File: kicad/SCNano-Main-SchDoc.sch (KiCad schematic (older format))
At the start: 26 parts, among them CON1 SC_CON_GEIGIE_4PIN, IC1 SN74LV4052A, Q1 STU85N3LH5, Q2 STU85N3LH5, Q3 STU85N3LH5, Q4 STU85N3LH5, SW1 SW-DPDT

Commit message: Remove alternate-mode symbols in RedBear Altium schematic symbols to prevent overlapped symbols in converted KiCAD schematic
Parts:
- removed IC12: (no value), symbol CAP_POL_RB13-25
- added 3V3, 3V3_10, 3V3_11, 3V3_2, 3V3_3, 3V3_4, 3V3_5, 3V3_6, 3V3_7, 3V3_8, 3V3_9: +3V3, symbol 3V3
- added GND, GND_10, GND_11, GND_12, GND_13, GND_14, GND_15, GND_2, GND_3, GND_4, GND_5, GND_6, GND_7, GND_8, GND_9: +GND, symbol GND
- added IC: (no value), symbol CAP_POL_RB13-25
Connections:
- net labels removed: +3V3, +GND

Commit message: Some more fixes for symbol related issues
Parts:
- removed 3V3, 3V3_10, 3V3_11, 3V3_2, 3V3_3, 3V3_4, 3V3_5, 3V3_6, 3V3_7, 3V3_8, 3V3_9: +3V3, symbol 3V3
- removed GND, GND_10, GND_11, GND_12, GND_13, GND_14, GND_15, GND_2, GND_3, GND_4, GND_5, GND_6, GND_7, GND_8, GND_9: +GND, symbol GND
- removed IC: (no value), symbol CAP_POL_RB13-25
- removed SOLARPANEL: VOLTAIC_SOLAR_PANEL_1W, symbol VOLTAIC_SOLAR_PANEL_1W
- added C1: CAP POL RB13-25, symbol CAP_POL_RB13-25
- added SOLARPANEL1: VOLTAIC_SOLAR_PANEL_1W, symbol VOLTAIC_SOLAR_PANEL_1W
- J1: value (none) -> ~
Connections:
- net labels added: +3V3, +GND
- wire segments 135 -> 122

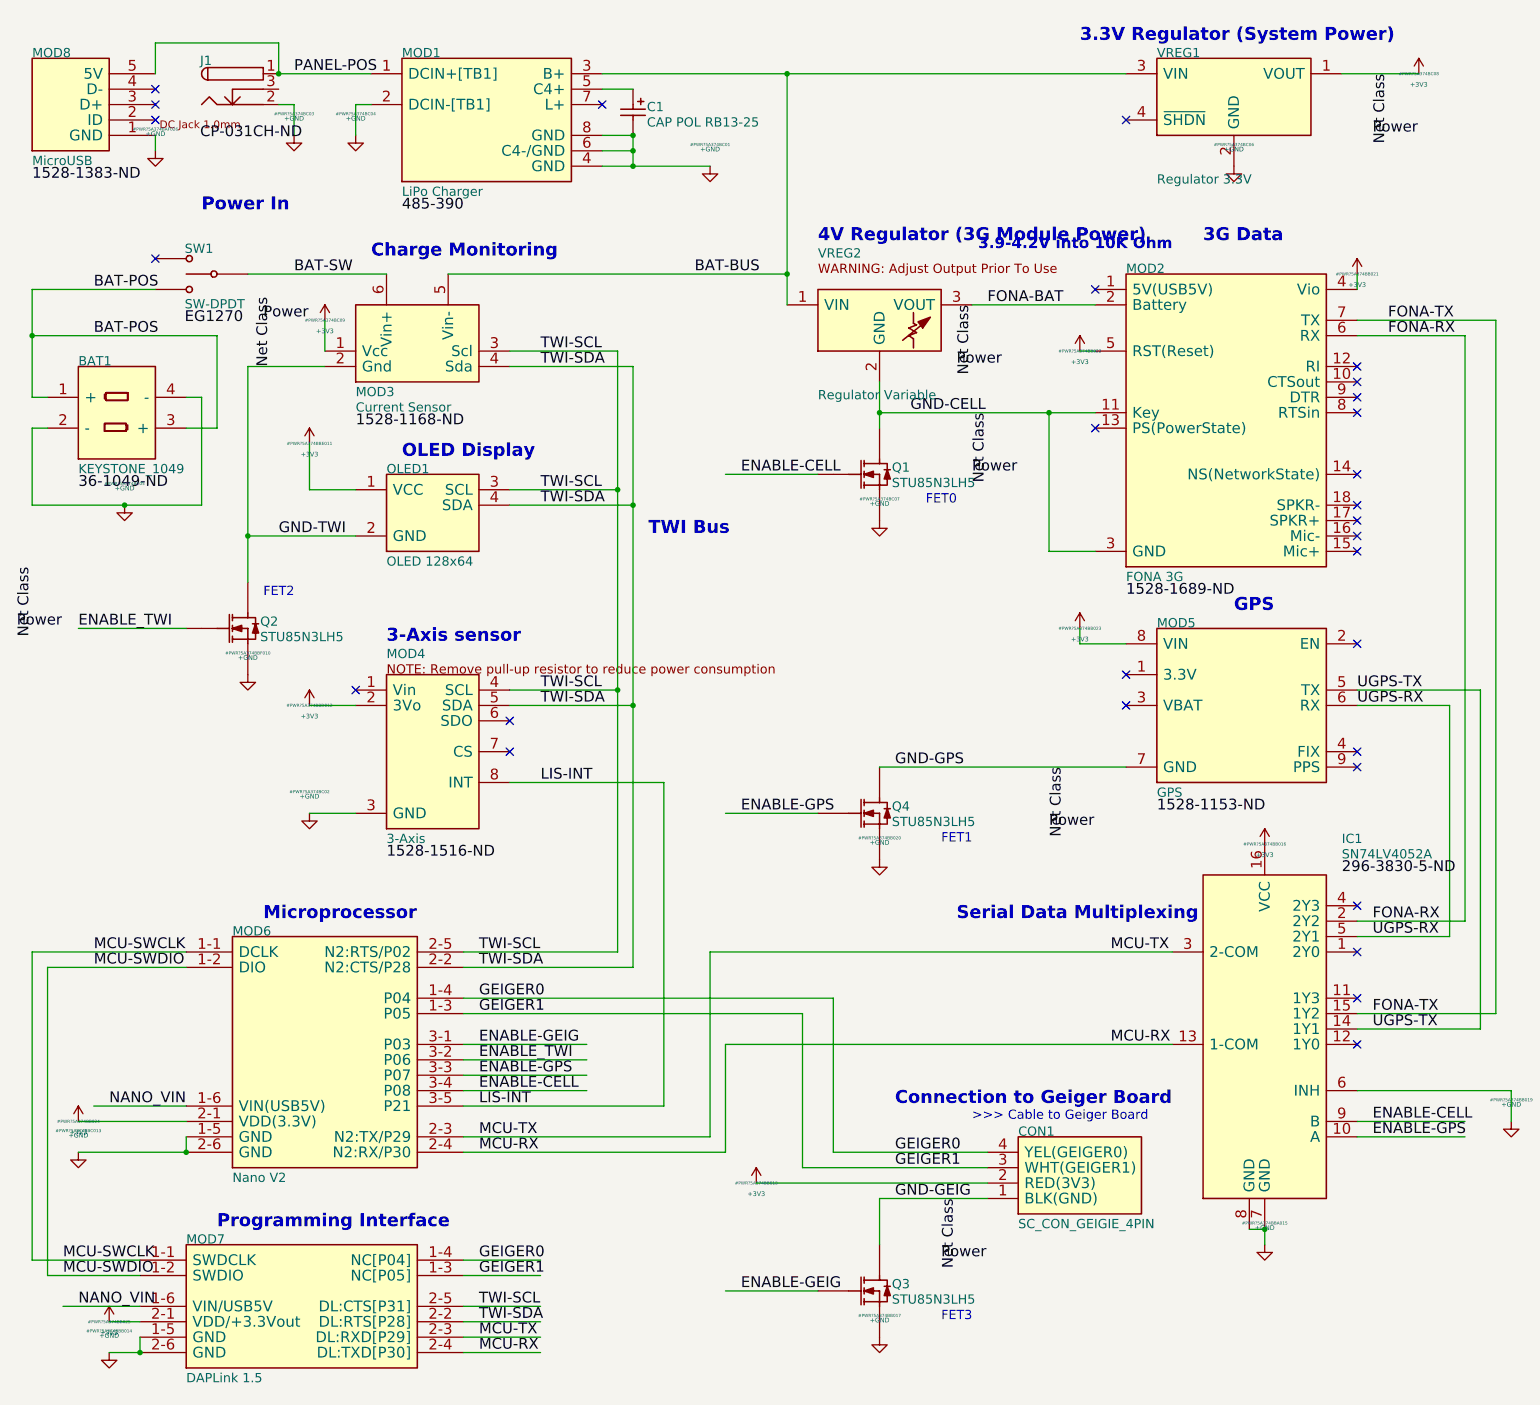
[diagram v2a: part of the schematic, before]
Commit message: Altium Class Name directives are unsupported in KiCAD. The conversion process placed the same ClassName directives as labels, which caused multiple nets to be treated as the same net.  Changed those labels into texts.
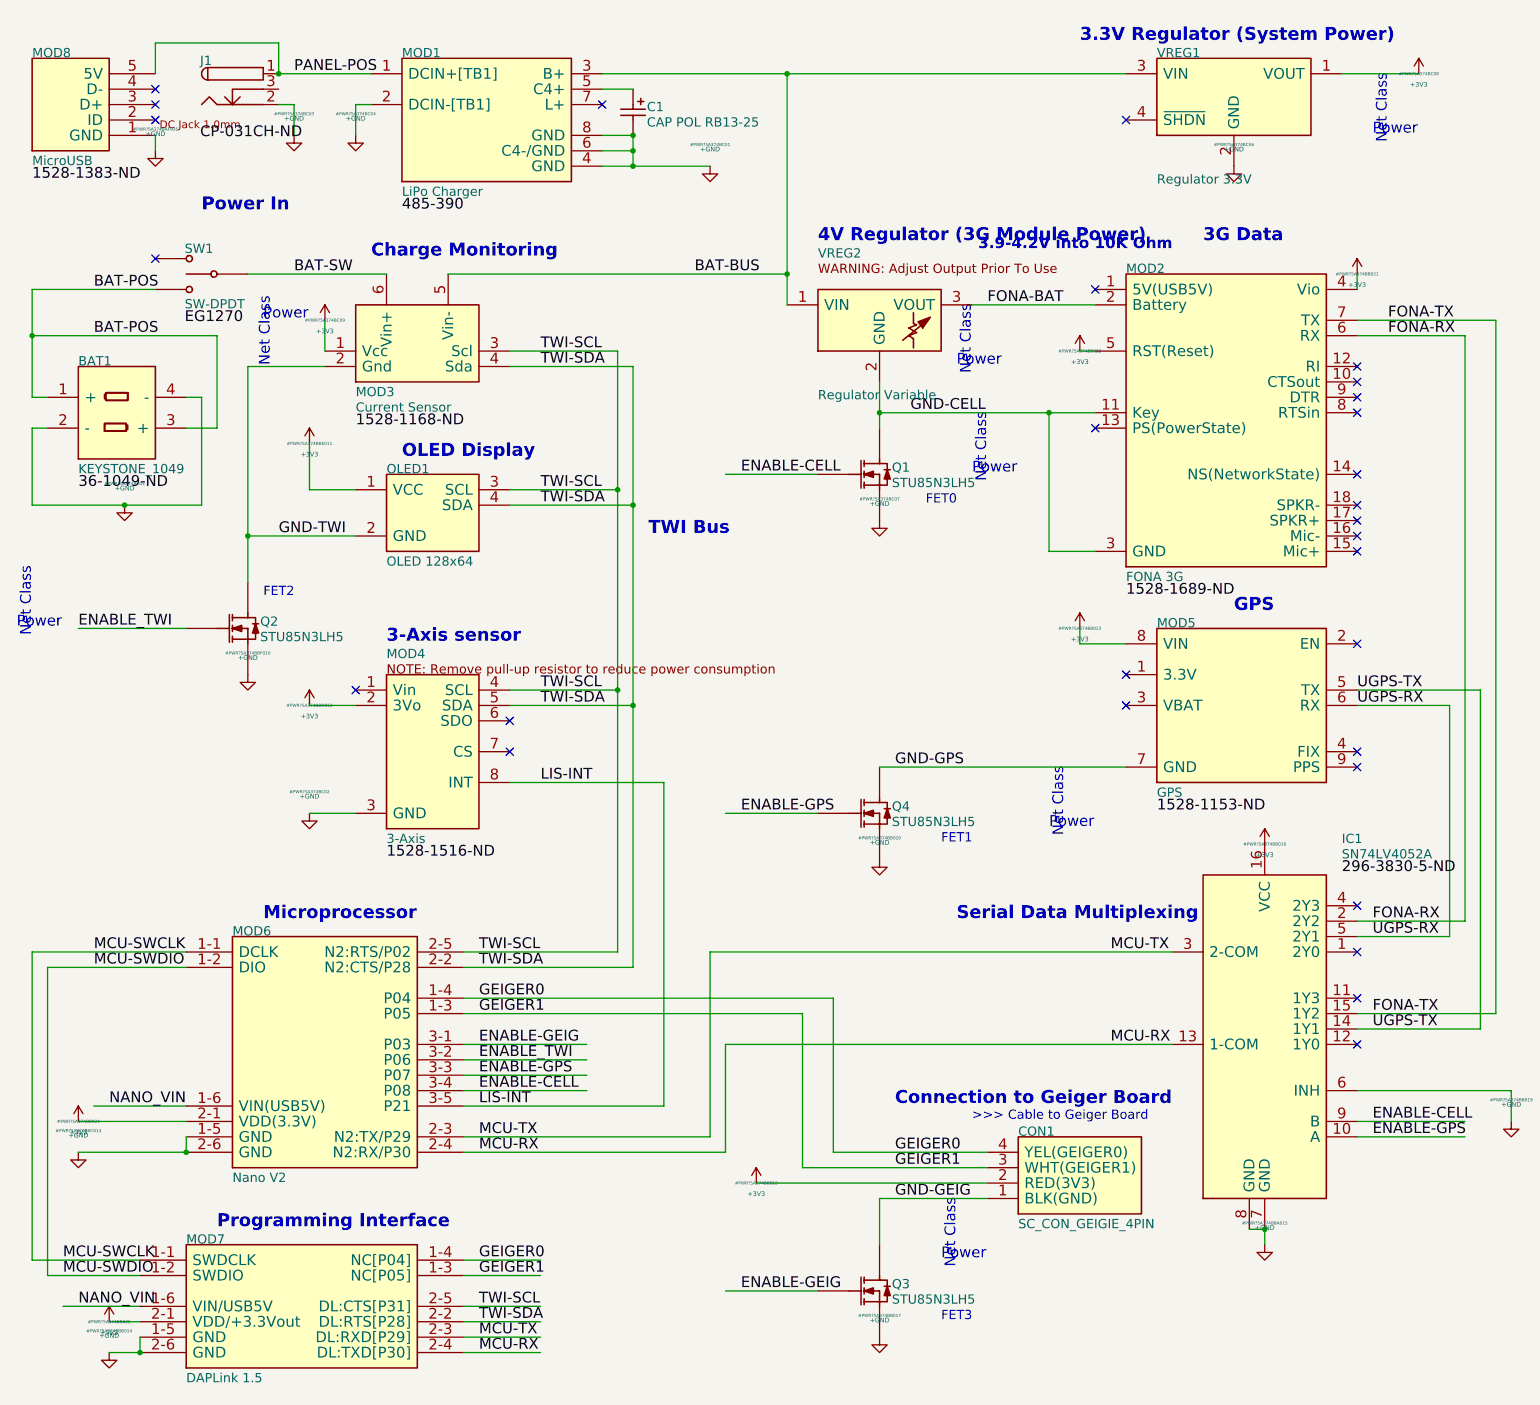
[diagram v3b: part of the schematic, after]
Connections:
- net labels removed: Net Class, Power
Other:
- note added: "Net Class"
- note added: "Power"
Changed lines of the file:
@@
 Text Notes 10800 6200 0    60   ~ 0
 Note: Grove 4-pin cable connects mainboard to geiger assembly.
-Text Label 6600 4300 3    70   ~ 0
-Net Class
-Text Label 6500 4700 0    70   ~ 0
-Power
-Text Label 6500 3600 3    70   ~ 0
-Net Class
-Text Label 6400 4000 0    70   ~ 0
-Power
-Text Label 7100 6600 3    70   ~ 0
-Net Class
-Text Label 7000 7000 0    70   ~ 0
-Power
-Text Label 9200 2100 3    70   ~ 0
-Net Class
-Text Label 9100 2500 0    70   ~ 0
-Power
 Text Label 2800 3000 0    70   ~ 0
 485-390
-Text Label 400  5300 3    70   ~ 0
-Net Class
-Text Label 300  5700 0    70   ~ 0
-Power
-Text Label 6400 9400 3    70   ~ 0
-Net Class
-Text Label 6300 9800 0    70   ~ 0
-Power
 Text Label 6000 9400 0    70   ~ 0
 GND-GEIG
@@
 Text Notes 10800 8500 0    60   ~ 0
 ToDo: Improved Pancake Tape Alignment Fixture
-Text Label 1950 4000 1    70   ~ 0
-Net Class
-Text Label 1900 3700 0    70   ~ 0
-Power
 Text Label 3300 10200 0    70   ~ 0
 TWI-SDA
@@
 	1    0    0    -1
 $EndComp
+Text Notes 6500 3600 3    70   ~ 0
+Net Class
+Text Notes 6600 4300 3    70   ~ 0
+Net Class
+Text Notes 7100 6600 3    70   ~ 0
+Net Class
+Text Notes 9200 2100 3    70   ~ 0
+Net Class
+Text Notes 400  5300 3    70   ~ 0
+Net Class
+Text Notes 6400 9400 3    70   ~ 0
+Net Class
+Text Notes 1950 4000 1    70   ~ 0
+Net Class
+Text Notes 6500 4700 0    70   ~ 0
+Power
+Text Notes 6400 4000 0    70   ~ 0
+Power
+Text Notes 7000 7000 0    70   ~ 0
+Power
+Text Notes 9100 2500 0    70   ~ 0
+Power
+Text Notes 300  5700 0    70   ~ 0
+Power
+Text Notes 6300 9800 0    70   ~ 0
+Power
+Text Notes 1900 3700 0    70   ~ 0
+Power
 $EndSCHEMATC
